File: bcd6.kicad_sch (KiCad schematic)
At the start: 0 parts

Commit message: added decoupling caps
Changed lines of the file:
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@@
+	)
+	(junction
+		(at 55.88 99.06)
+		(diameter 0)
+		(color 0 0 0 0)
 	)
 	(junction
@@
 	)
 	(junction
-		(at 55.88 99.06)
-		(diameter 0)
-		(color 0 0 0 0)
-	)
-	(junction
 		(at 90.17 113.03)
 		(diameter 0)
@@
 	)
 	(symbol
-		(lib_id "power:VDD")
+		(lib_id "power:+3V3")
 		(at 55.88 99.06 0)
 		(unit 1)
@@
 			)
 		)
-		(property "Value" "VDD"
+		(property "Value" "+3V3"
 			(at 55.88 94.9269 0)
 			(effects
@@
 			)
 		)
-		(property "Description" "Power symbol creates a global label with name \"VDD\""
+		(property "Description" "Power symbol creates a global label with name \"+3V3\""
 			(at 55.88 99.06 0)
 			(effects

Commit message: schematic cleanup, routed 1 bdc
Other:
- sheet NAND2: file and.kicad_sch -> nand.kicad_sch
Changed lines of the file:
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@@
 		(dnp no)
 		(fields_autoplaced yes)
-		(property "Reference" "#PWR0241"
+		(property "Reference" "#PWR0233"
 			(at 55.88 102.87 0)
 			(effects
@@
 			(project "transistor-clock"
 				(path "/ce10d5bc-995e-4952-aa76-0a08f713a0f2/2c36a9e9-de42-4705-9ad4-94f4cc168e2f/45f6b4b3-4b31-405d-8488-938c33278b8a"
-					(reference "#PWR0365")
+					(reference "#PWR0261")
 					(unit 1)
 				)
 				(path "/ce10d5bc-995e-4952-aa76-0a08f713a0f2/2c36a9e9-de42-4705-9ad4-94f4cc168e2f/6e22859f-9bca-4d3f-9901-b092abdf20a9"
-					(reference "#PWR0241")
+					(reference "#PWR0233")
 					(unit 1)
 				)
@@
 			)
 		)
-		(property "Sheetfile" "and.kicad_sch"
+		(property "Sheetfile" "nand.kicad_sch"
 			(at 152.4 98.3746 0)
 			(effects

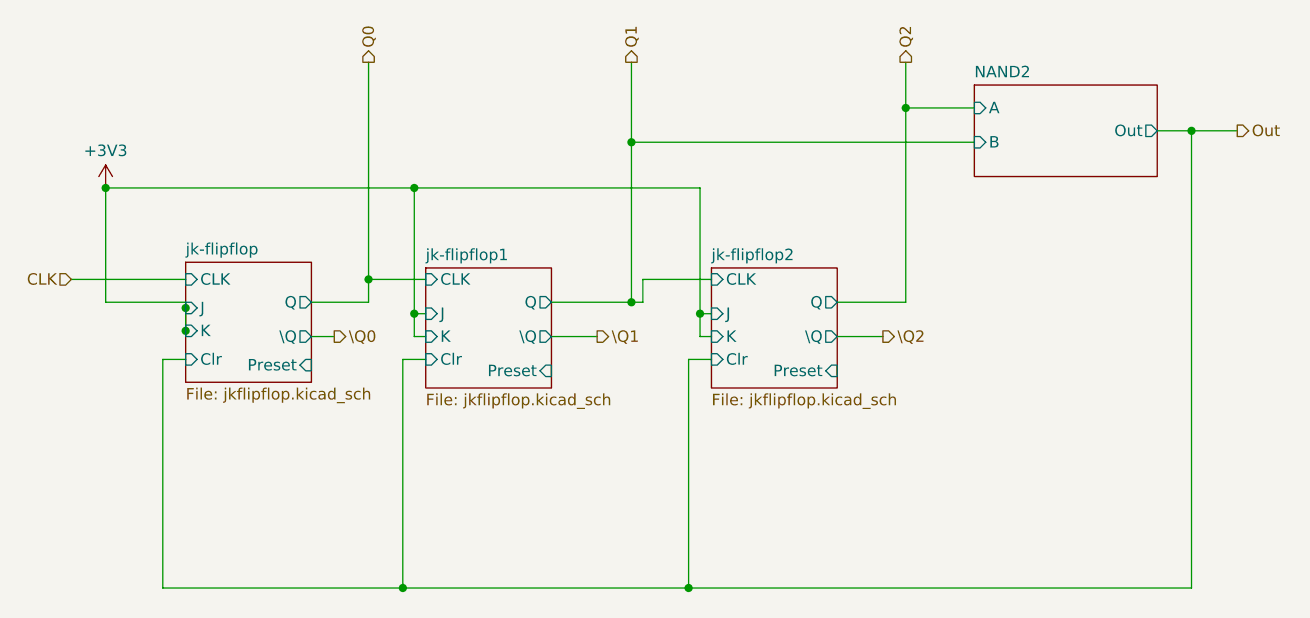
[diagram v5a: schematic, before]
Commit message: switched to using flipflop module
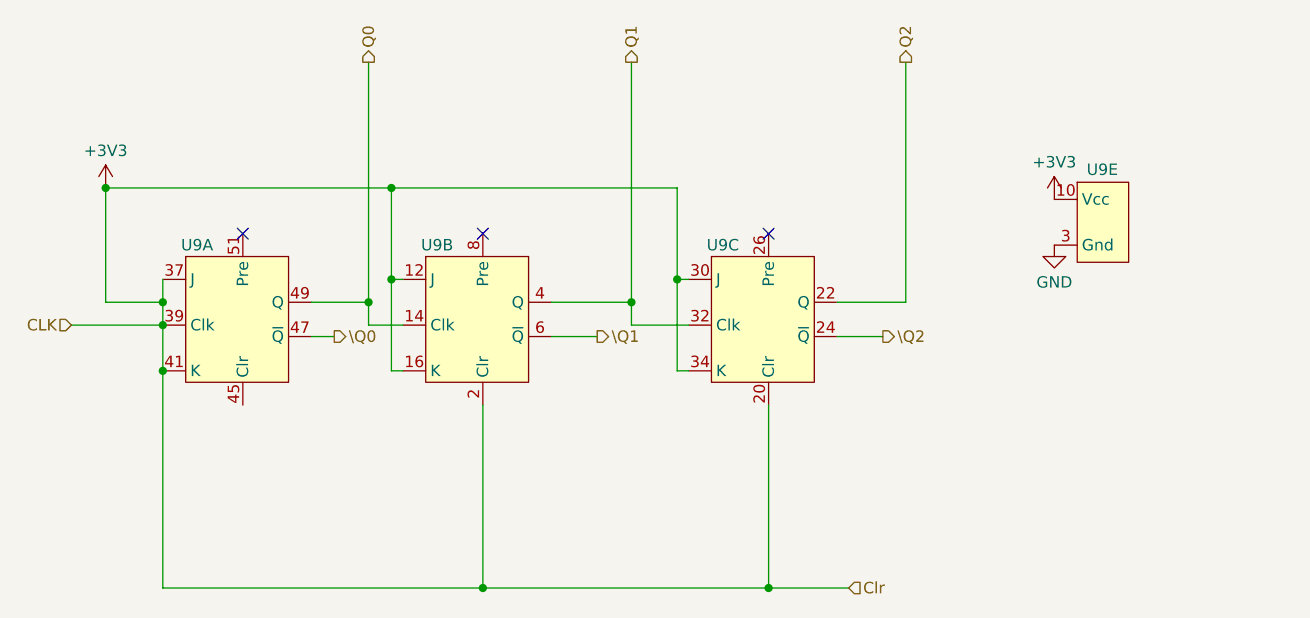
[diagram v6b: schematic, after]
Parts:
- added U9: ~, symbol custom:jk-flipflops
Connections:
- net +3V3: now also U9.10 (Vcc), U9.12 (J), U9.16 (K), U9.18 (Vcc), U9.2 (Clr), U9.20 (Clr), U9.28 (Vcc), U9.30 (J), U9.34 (K), U9.36 (Vcc), U9.37 (J), U9.39 (Clk), U9.41 (K), U9.46 (Vcc)
- net Q0: now also U9.14 (Clk), U9.49 (Q)
- net Q1: now also U9.32 (Clk), U9.4 (Q)
- net Q2: now also U9.22 (Q)
- net \Q0: now also U9.47 (~{Q})
- net \Q1: now also U9.6 (~{Q})
- net \Q2: now also U9.24 (~{Q})
- new net GND: U9.19 (Gnd), U9.27 (Gnd), U9.3 (Gnd), U9.43 (Gnd), U9.9 (Gnd)
- no-connect marks 0 -> 3
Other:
- removed sheet NAND2
- removed sheet jk-flipflop
- removed sheet jk-flipflop1
- removed sheet jk-flipflop2
